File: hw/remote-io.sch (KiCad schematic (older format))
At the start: 13 parts, among them P1 CONN_01X02, P10 CONN_01X04, P2 CONN_01X08, P3 CONN_01X08, P5 CONN_02X20

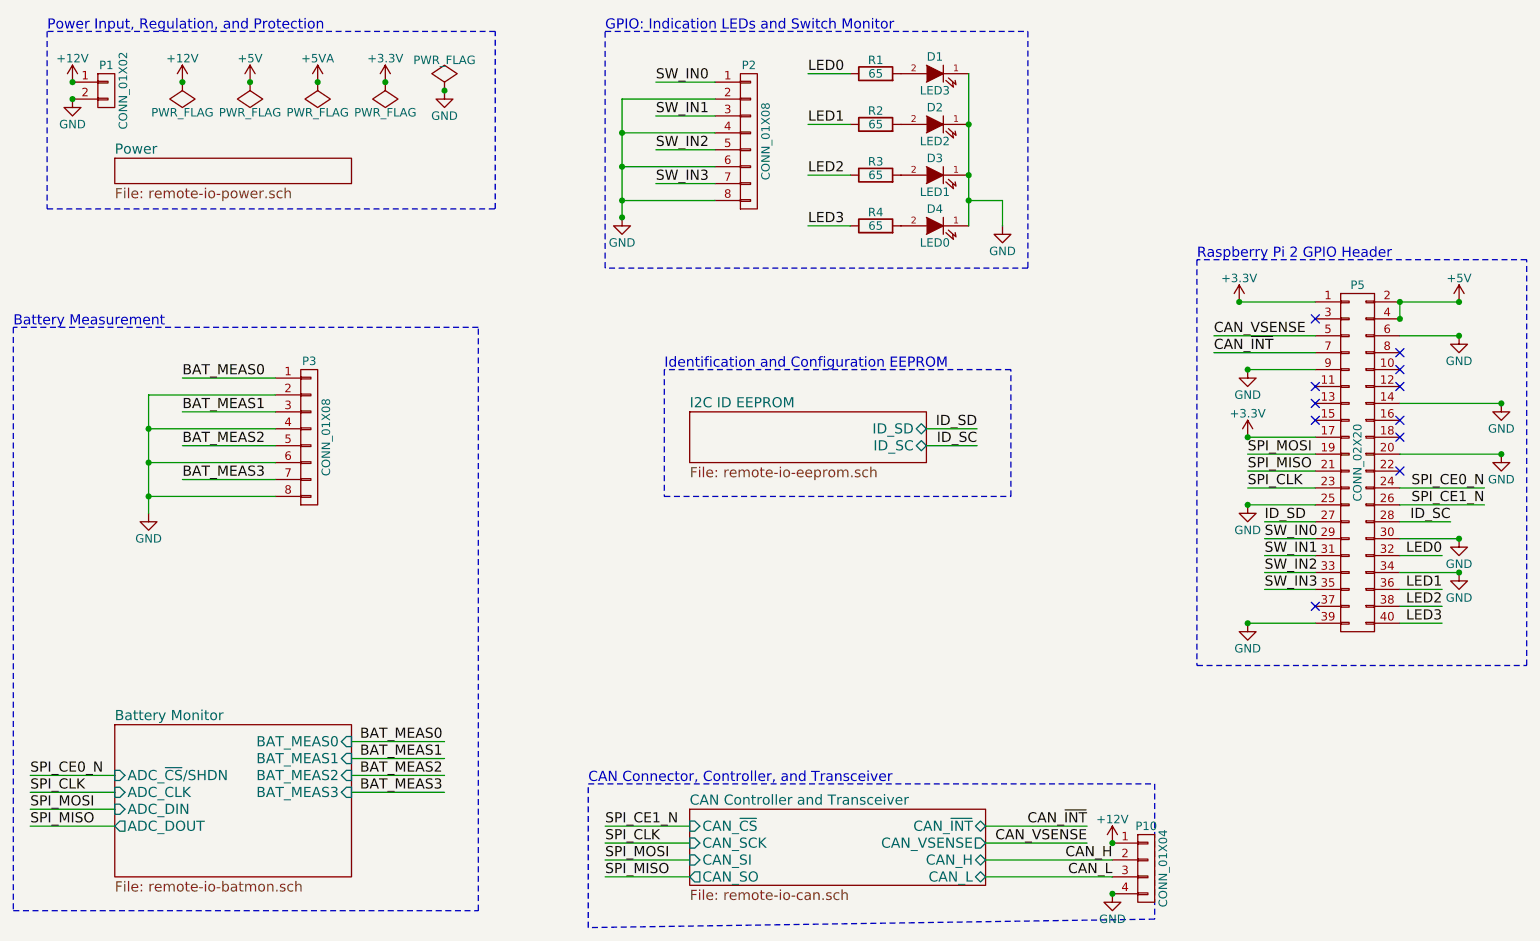
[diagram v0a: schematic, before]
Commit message: Isolated CAN bus connections and added proper mounting holes
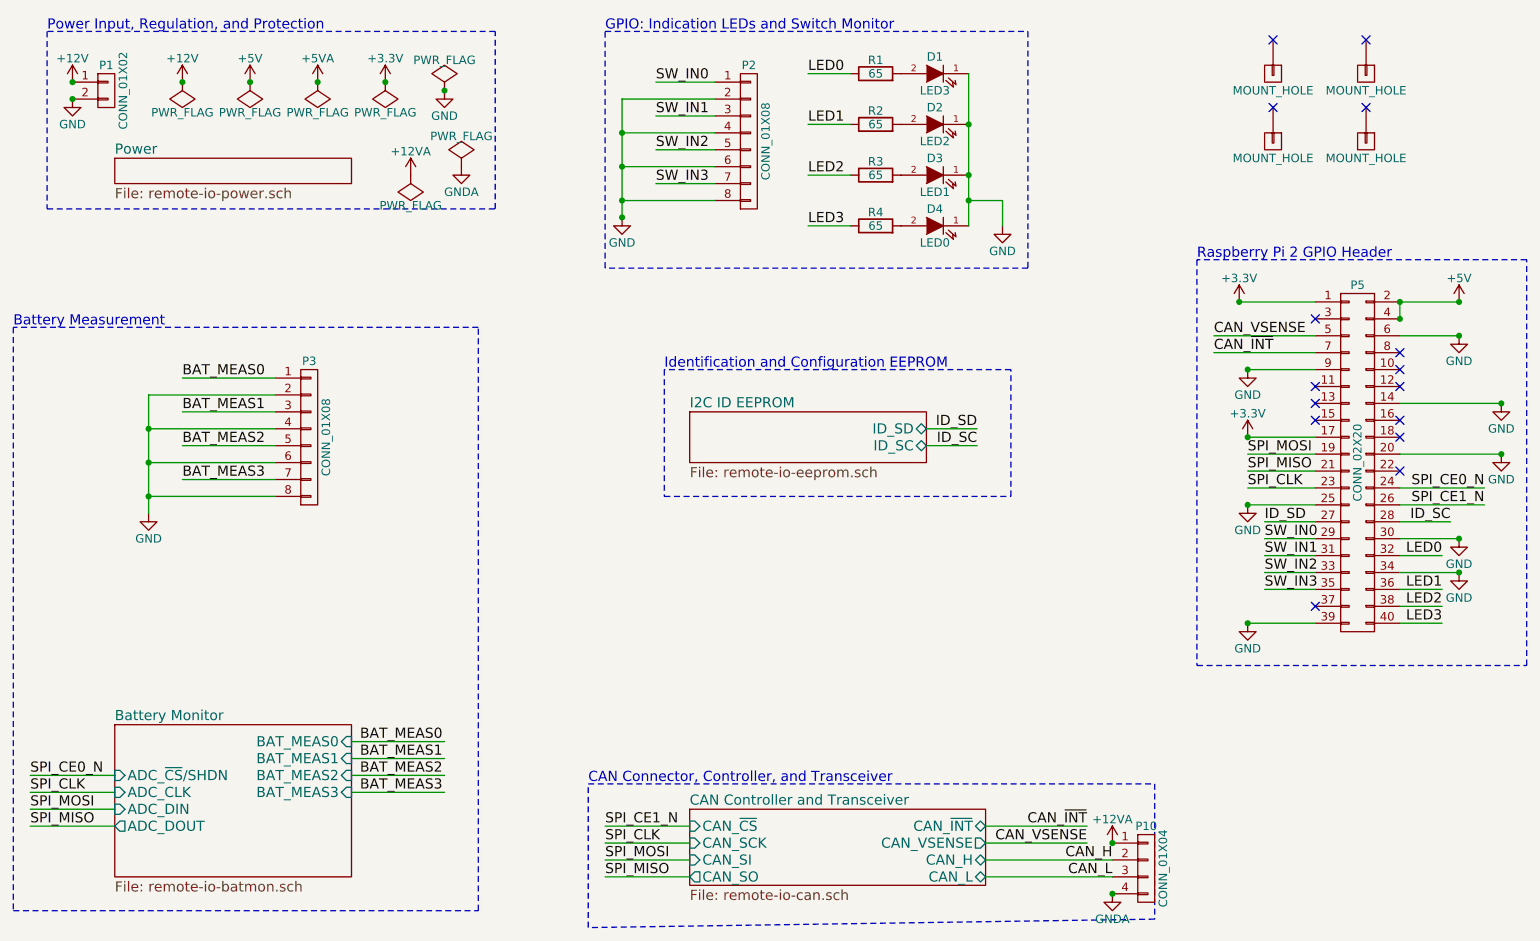
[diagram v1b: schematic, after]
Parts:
- added H1, H2, H3, H4: MOUNT_HOLE, Mounting_Holes:MountingHole_2-7mm, symbol MOUNT_HOLE
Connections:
- net labels added: +12VA, GNDA
- no-connect marks 11 -> 15
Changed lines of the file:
@@
 EESchema Schematic File Version 2
+LIBS:remote-io-rescue
 LIBS:power
 LIBS:device
@@
 $EndComp
 $Comp
-L +12V #PWR027
-U 1 1 5588C988
+L +12VA #PWR027
+U 1 1 558B5104
 P 7550 5800
 F 0 "#PWR027" H 7550 5650 50  0001 C CNN
-F 1 "+12V" H 7550 5940 50  0000 C CNN
+F 1 "+12VA" H 7550 5940 50  0000 C CNN
 F 2 "" H 7550 5800 60  0000 C CNN
 F 3 "" H 7550 5800 60  0000 C CNN
@@
 $EndComp
 $Comp
-L GND #PWR028
-U 1 1 5588CAFD
+L GNDA #PWR028
+U 1 1 558B519E
 P 7550 6100
 F 0 "#PWR028" H 7550 5850 50  0001 C CNN
-F 1 "GND" H 7550 5950 50  0000 C CNN
+F 1 "GNDA" H 7550 5950 50  0000 C CNN
 F 2 "" H 7550 6100 60  0000 C CNN
 F 3 "" H 7550 6100 60  0000 C CNN
@@
 Connection ~ 7550 5800
 Connection ~ 7550 6100
+$Comp
+L +12VA #PWR029
+U 1 1 558B6E45
+P 3400 1850
+F 0 "#PWR029" H 3400 1700 50  0001 C CNN
+F 1 "+12VA" H 3400 1990 50  0000 C CNN
+F 2 "" H 3400 1850 60  0000 C CNN
+F 3 "" H 3400 1850 60  0000 C CNN
+	1    3400 1850
+	1    0    0    -1
+$EndComp
+$Comp
+L GNDA #PWR030
+U 1 1 558B6EDF
+P 3700 1800
+F 0 "#PWR030" H 3700 1550 50  0001 C CNN
+F 1 "GNDA" H 3700 1650 50  0000 C CNN
+F 2 "" H 3700 1800 60  0000 C CNN
+F 3 "" H 3700 1800 60  0000 C CNN
+	1    3700 1800
+	1    0    0    -1
+$EndComp
+$Comp
+L PWR_FLAG #FLG031
+U 1 1 558B6F84
+P 3400 1850
+F 0 "#FLG031" H 3400 1945 50  0001 C CNN
+F 1 "PWR_FLAG" H 3400 2030 50  0000 C CNN
+F 2 "" H 3400 1850 60  0000 C CNN
+F 3 "" H 3400 1850 60  0000 C CNN
+	1    3400 1850
+	-1   0    0    1
+$EndComp
+$Comp
+L PWR_FLAG #FLG032
+U 1 1 558B7022
+P 3700 1800
+F 0 "#FLG032" H 3700 1895 50  0001 C CNN
+F 1 "PWR_FLAG" H 3700 1980 50  0000 C CNN
+F 2 "" H 3700 1800 60  0000 C CNN
+F 3 "" H 3700 1800 60  0000 C CNN
+	1    3700 1800
+	1    0    0    -1
+$EndComp
+$Comp
+L MOUNT_HOLE H1
+U 1 1 558B91CD
+P 8500 1250
+F 0 "H1" H 8500 1350 50  0001 C CNN
+F 1 "MOUNT_HOLE" V 8600 1250 50  0000 C CNN
+F 2 "Mounting_Holes:MountingHole_2-7mm" H 8500 1250 60  0001 C CNN
+F 3 "" H 8500 1250 60  0000 C CNN
+	1    8500 1250
+	0    1    1    0
+$EndComp
+NoConn ~ 8500 1050
+$Comp
+L MOUNT_HOLE H3
+U 1 1 558BA608
+P 8500 1650
+F 0 "H3" H 8500 1750 50  0001 C CNN
+F 1 "MOUNT_HOLE" V 8600 1650 50  0000 C CNN
+F 2 "Mounting_Holes:MountingHole_2-7mm" H 8500 1650 60  0001 C CNN
+F 3 "" H 8500 1650 60  0000 C CNN
+	1    8500 1650
+	0    1    1    0
+$EndComp
+NoConn ~ 8500 1450
+$Comp
+L MOUNT_HOLE H2
+U 1 1 558BA8B3
+P 9050 1250
+F 0 "H2" H 9050 1350 50  0001 C CNN
+F 1 "MOUNT_HOLE" V 9150 1250 50  0000 C CNN
+F 2 "Mounting_Holes:MountingHole_2-7mm" H 9050 1250 60  0001 C CNN
+F 3 "" H 9050 1250 60  0000 C CNN
+	1    9050 1250
+	0    1    1    0
+$EndComp
+NoConn ~ 9050 1050
+$Comp
+L MOUNT_HOLE H4
+U 1 1 558BA8BA
+P 9050 1650
+F 0 "H4" H 9050 1750 50  0001 C CNN
+F 1 "MOUNT_HOLE" V 9150 1650 50  0000 C CNN
+F 2 "Mounting_Holes:MountingHole_2-7mm" H 9050 1650 60  0001 C CNN
+F 3 "" H 9050 1650 60  0000 C CNN
+	1    9050 1650
+	0    1    1    0
+$EndComp
+NoConn ~ 9050 1450
 $EndSCHEMATC

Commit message: Finished rev 0 with gerbers and drills
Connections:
- wire segments 72 -> 71
- no-connect marks 15 -> 16
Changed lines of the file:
@@
-$EndComp
-$Comp
-L +3.3V #PWR07
-U 1 1 557F877D
-P 8350 3400
-F 0 "#PWR07" H 8350 3250 50  0001 C CNN
-F 1 "+3.3V" H 8350 3540 50  0000 C CNN
-F 2 "" H 8350 3400 60  0000 C CNN
-F 3 "" H 8350 3400 60  0000 C CNN
-	1    8350 3400
-	1    0    0    -1
 $EndComp
 $Comp
@@
 	9250 2600 9600 2600
 Wire Wire Line
-	9250 2800 9600 2800
-Wire Wire Line
 	9250 4200 9600 4200
-Wire Wire Line
-	8350 3400 8750 3400
 Wire Wire Line
 	8750 3800 8350 3800
@@
 Connection ~ 8300 2600
 Connection ~ 8350 3000
-Connection ~ 8350 3400
 Connection ~ 8350 3800
 Connection ~ 8350 4500
@@
 $EndComp
 NoConn ~ 9050 1450
+Wire Wire Line
+	9250 2800 9600 2800
+NoConn ~ 8750 3400
 $EndSCHEMATC

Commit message: Added PCB and schematic prints
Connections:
- wire segments 71 -> 80
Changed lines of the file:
@@
 L GND #PWR013
 U 1 1 558298A3
-P 9850 3200
-F 0 "#PWR013" H 9850 2950 50  0001 C CNN
-F 1 "GND" H 9850 3050 50  0000 C CNN
-F 2 "" H 9850 3200 60  0000 C CNN
-F 3 "" H 9850 3200 60  0000 C CNN
-	1    9850 3200
+P 9600 3200
+F 0 "#PWR013" H 9600 2950 50  0001 C CNN
+F 1 "GND" H 9600 3050 50  0000 C CNN
+F 2 "" H 9600 3200 60  0000 C CNN
+F 3 "" H 9600 3200 60  0000 C CNN
+	1    9600 3200
 	1    0    0    -1
 $EndComp
@@
 	9250 4500 9500 4500
 Wire Wire Line
-	6700 1250 6700 2150
+	6700 1250 6700 1550
+Wire Wire Line
+	6700 1550 6700 1850
+Wire Wire Line
+	6700 1850 6700 2000
+Wire Wire Line
+	6700 2000 6700 2150
 Connection ~ 6700 1550
 Connection ~ 6700 1850
@@
 	9250 2700 9250 2600
 Wire Wire Line
-	9250 3200 9850 3200
+	9250 3200 9600 3200
 Wire Wire Line
 	9250 3500 9850 3500
@@
 	10000 2350 8050 2350
 Wire Wire Line
-	1850 3150 1850 3850
+	1850 3150 1850 3350
+Wire Wire Line
+	1850 3350 1850 3550
+Wire Wire Line
+	1850 3550 1850 3750
+Wire Wire Line
+	1850 3750 1850 3850
 Connection ~ 1850 3350
 Connection ~ 1850 3550
@@
 	6800 6000 7550 6000
 Wire Notes Line
-	4450 5450 7800 5450
-Wire Notes Line
-	7800 5450 7800 6250
-Wire Notes Line
-	7800 6250 4450 6300
+	4450 5450 8000 5450
+Wire Notes Line
+	8000 5450 8000 6300
+Wire Notes Line
+	8000 6300 4450 6300
 Wire Notes Line
 	4450 6300 4450 5450
@@
 Connection ~ 9600 4200
 Connection ~ 9850 3500
-Connection ~ 9850 3200
+Connection ~ 9600 3200
 Connection ~ 9600 2600
 Connection ~ 9600 2800
@@
 $EndComp
 Wire Wire Line
-	4650 1400 4650 2100
+	4650 1400 4650 1600
+Wire Wire Line
+	4650 1600 4650 1800
+Wire Wire Line
+	4650 1800 4650 2000
+Wire Wire Line
+	4650 2000 4650 2100
 Connection ~ 4650 1600
 Connection ~ 4650 1800
